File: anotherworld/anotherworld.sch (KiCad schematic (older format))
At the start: 0 parts

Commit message: lots of stuff :-)
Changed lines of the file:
@@
 $Descr A4 11693 8268
 encoding utf-8
-Sheet 1 9
+Sheet 1 8
 Title ""
 Date "8 aug 2016"
@@
 $EndDescr
 $Sheet
-S 1700 2200 1450 350
+S 1250 1150 1450 350
 U 57A22D3F
 F0 "JAMMA Connector" 50
@@
 $EndSheet
 $Sheet
-S 1700 2800 1450 350
+S 1250 1750 1450 350
 U 57A22D68
 F0 "Instruction Decoder" 50
@@
 $EndSheet
 $Sheet
-S 1700 3400 1450 350
+S 1250 2350 1450 350
 U 57A248D2
 F0 "Master Clock" 50
@@
 $EndSheet
 $Sheet
-S 1700 4000 1450 350
-U 57A24908
-F0 "Jump Instructions Decoder" 50
-F1 "jump_decoder.sch" 50
-$EndSheet
-$Sheet
-S 1700 4600 1450 300
-U 57A24939
-F0 "Registers" 50
-F1 "registers.sch" 50
-$EndSheet
-$Sheet
-S 1700 5100 1450 350
+S 1250 2950 1450 350
 U 57A2BA94
 F0 "Stack" 50
@@
 $EndSheet
 $Sheet
-S 1700 5650 1450 300
+S 1250 3500 1450 300
 U 57A4B50B
 F0 "Arithmetic & Logic Unit" 50
@@
 $EndSheet
 $Sheet
-S 1700 6200 1450 300
+S 1250 4050 1450 300
 U 57A82FBD
 F0 "Code ROM Banks & Instruction Pointers" 50
 F1 "code_banks.sch" 50
 $EndSheet
+$Sheet
+S 1250 4550 1450 300
+U 57A7E619
+F0 "Microcode ROM" 50
+F1 "microcode.sch" 50
+$EndSheet
 $EndSCHEMATC

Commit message: SRAM sheet
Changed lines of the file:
@@
 Sheet 1 8
 Title ""
-Date "8 aug 2016"
+Date "9 aug 2016"
 Rev ""
 Comp ""
@@
 S 1250 2950 1450 350
 U 57A2BA94
-F0 "Stack" 50
-F1 "stack.sch" 50
+F0 "Static RAM (VM vars + STACK + CHAN_PTRs + SCRATCHPAD)" 50
+F1 "sram.sch" 50
 $EndSheet
 $Sheet

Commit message: weekly workshop update
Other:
- note added: "* 16bit ALU\n* ALU Input Registers\n* ALU Output Latches"
- note added: "* Code ROM\n* Instruction Pointer Register\n* ROM Bank Register"
- note added: "* Microcode ROMs\n* Opcode Register"
- note added: "* Stack area\n* Channel Pointers\n* "VM" vars (i.e. system RAM)\n* Scratchpad area"
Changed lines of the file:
@@
 LIBS:valves
 LIBS:27c801
+LIBS:o_ttl
 LIBS:anotherworld-cache
 EELAYER 27 0
@@
 $Descr A4 11693 8268
 encoding utf-8
-Sheet 1 8
+Sheet 1 7
 Title ""
 Date "9 aug 2016"
@@
 $EndDescr
 $Sheet
-S 1250 1150 1450 350
+S 3100 2700 1450 350
 U 57A22D3F
 F0 "JAMMA Connector" 50
@@
 $EndSheet
 $Sheet
-S 1250 1750 1450 350
-U 57A22D68
-F0 "Instruction Decoder" 50
-F1 "instruction_decoder.sch" 50
-$EndSheet
-$Sheet
-S 1250 2350 1450 350
+S 3100 3250 1450 350
 U 57A248D2
 F0 "Master Clock" 50
@@
 $EndSheet
 $Sheet
-S 1250 2950 1450 350
+S 1250 2700 1600 500
 U 57A2BA94
-F0 "Static RAM (VM vars + STACK + CHAN_PTRs + SCRATCHPAD)" 50
+F0 "Static RAM" 50
 F1 "sram.sch" 50
 $EndSheet
 $Sheet
-S 1250 3500 1450 300
+S 1250 3450 1600 400
 U 57A4B50B
 F0 "Arithmetic & Logic Unit" 50
@@
 $EndSheet
 $Sheet
-S 1250 4050 1450 300
+S 1250 4750 1600 300
+U 57A7E619
+F0 "Microcode Sequencer" 50
+F1 "microcode.sch" 50
+$EndSheet
+$Sheet
+S 1250 4100 1600 400
 U 57A82FBD
-F0 "Code ROM Banks & Instruction Pointers" 50
+F0 "Code ROM Banks" 50
 F1 "code_banks.sch" 50
 $EndSheet
-$Sheet
-S 1250 4550 1450 300
-U 57A7E619
-F0 "Microcode ROM" 50
-F1 "microcode.sch" 50
-$EndSheet
+Text Notes 1350 2850 0    60   ~ 0
+* Stack area\n* Channel Pointers\n* "VM" vars (i.e. system RAM)\n* Scratchpad area
+Text Notes 1350 4250 0    60   ~ 0
+* Code ROM\n* Instruction Pointer Register\n* ROM Bank Register
+Text Notes 1350 4900 0    60   ~ 0
+* Microcode ROMs\n* Opcode Register
+Text Notes 1350 3600 0    60   ~ 0
+* 16bit ALU\n* ALU Input Registers\n* ALU Output Latches
 $EndSCHEMATC

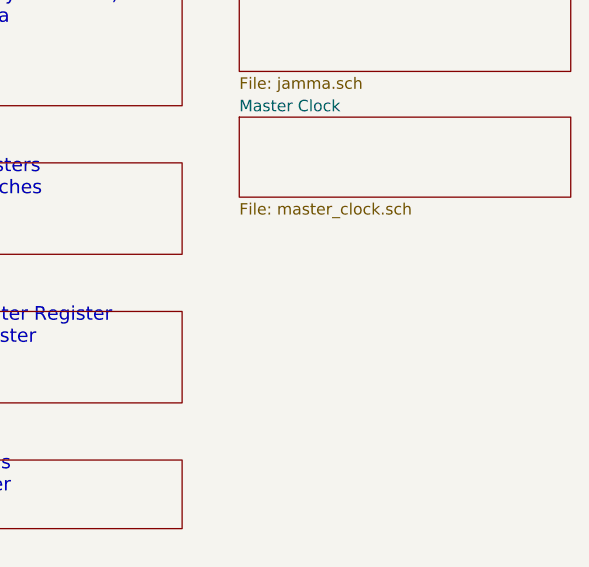
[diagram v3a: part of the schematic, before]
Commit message: palette selection and video output circuitry (Color DAC and Palette ROM)
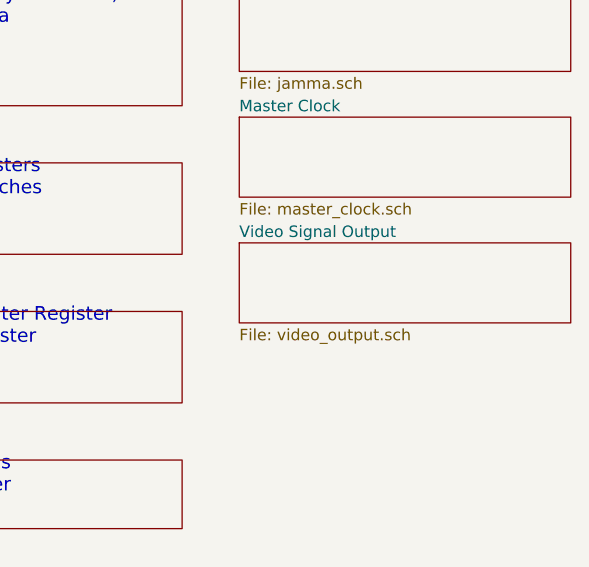
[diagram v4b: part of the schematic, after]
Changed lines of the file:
@@
 $Descr A4 11693 8268
 encoding utf-8
-Sheet 1 7
+Sheet 1 8
 Title ""
-Date "9 aug 2016"
+Date "10 aug 2016"
 Rev ""
 Comp ""
@@
 Text Notes 1350 3600 0    60   ~ 0
 * 16bit ALU\n* ALU Input Registers\n* ALU Output Latches
+$Sheet
+S 3100 3800 1450 350
+U 57AAB07E
+F0 "Video Signal Output" 50
+F1 "video_output.sch" 50
+$EndSheet
 $EndSCHEMATC
